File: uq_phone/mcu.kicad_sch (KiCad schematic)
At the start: 22 parts, among them J11 FTSH-105-XX-X-DV, U5 TXB0108RGYR, U6 TXB0108RGYR, U7 STM32H730VBTx

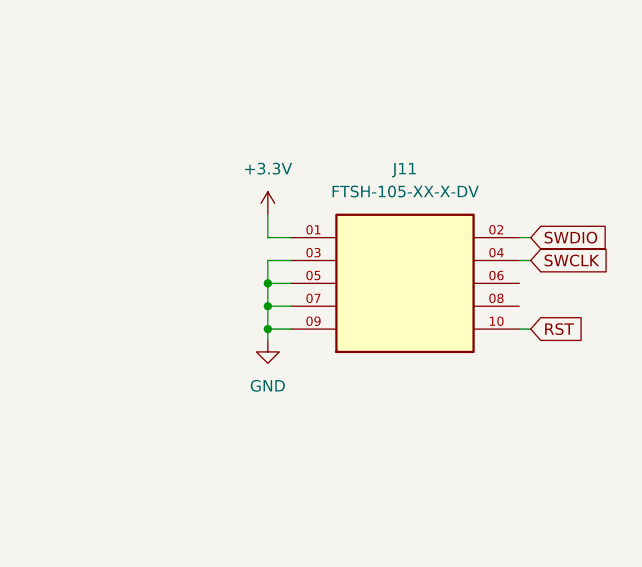
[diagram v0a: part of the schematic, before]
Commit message: Update LCD, Add Programer, Shrink Footprints
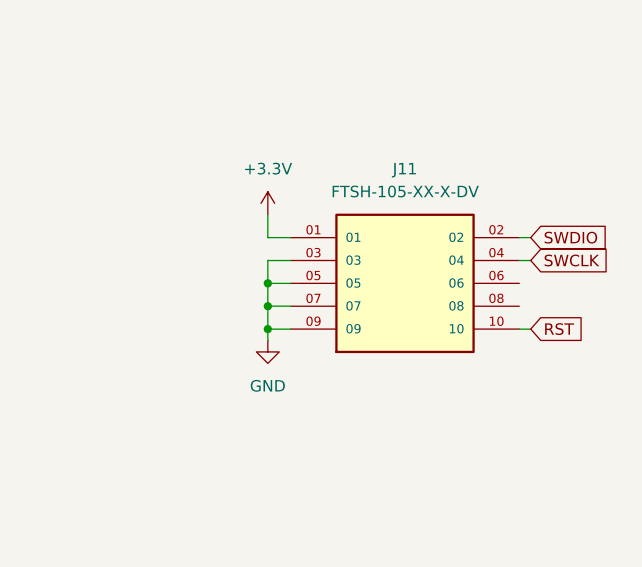
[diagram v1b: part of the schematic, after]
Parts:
- R26, R27, R28, R29: footprint Resistor_SMD:R_0603_1608Metric -> Resistor_SMD:R_0402_1005Metric

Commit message: Shrink More footprints, rearragment of PCB
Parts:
- C19, C20, C21, C22, C23, C24, C25, C26, C27, C28, C29, C30, C31: footprint Capacitor_SMD:C_0603_1608Metric -> Capacitor_SMD:C_0402_1005Metric

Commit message: Update PCB, minor changes
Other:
- note added: "CHECK PINOUT"
- note added: "MCU"
- note added: "Programmer"
- moved on the sheet: C19, C20, C21, C22, J11, U5, U6

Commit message: Arrange PCB
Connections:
- net MOB_PWR: no longer names the net of U7.93 (PB7)
- net MOB_RST renamed MOB_RST_CTL

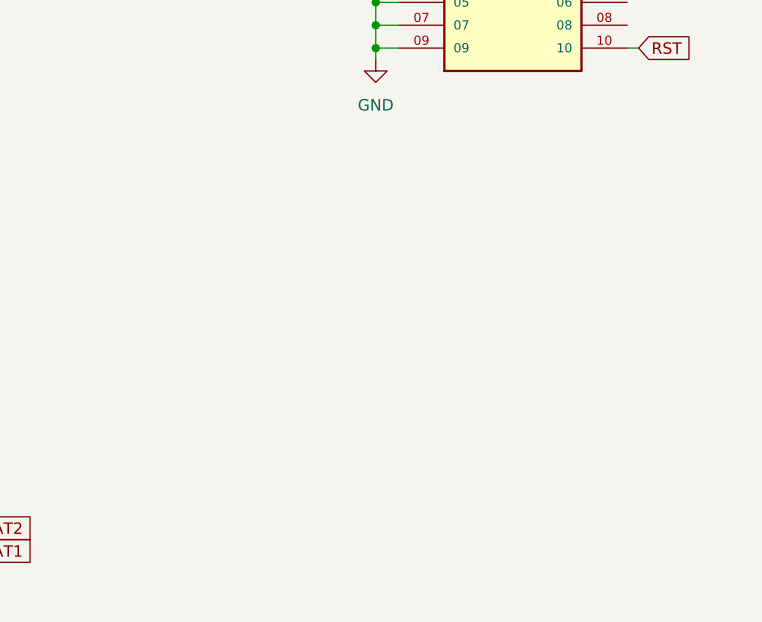
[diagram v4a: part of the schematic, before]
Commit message: Add LEDs, Inital Buttons
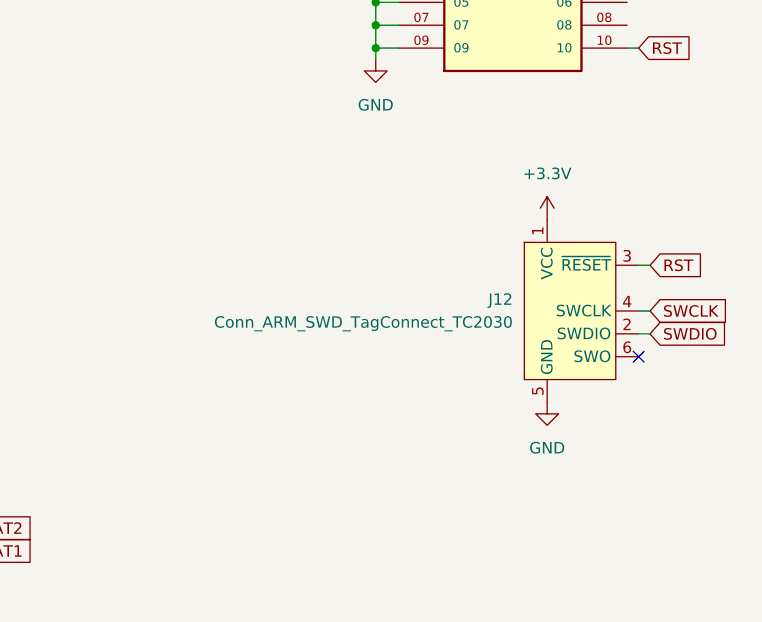
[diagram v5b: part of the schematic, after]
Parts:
- added J12: Conn_ARM_SWD_TagConnect_TC2030, Connector:Tag-Connect_TC2030-IDC-FP_2x03_P1.27mm_Vertical, symbol Connector:Conn_ARM_SWD_TagConnect_TC2030
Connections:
- net +3.3V: now also J12.1 (VCC)
- net GND: now also J12.5 (GND)
- net RST: now also J12.3 (~{RESET})
- net SWCLK: now also J12.4 (SWCLK)
- net SWDIO: now also J12.2 (SWDIO)
- no-connect marks 3 -> 4

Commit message: Routing Init
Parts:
- removed TP19: TestPoint, TestPoint:TestPoint_Pad_D1.0mm, symbol Connector:TestPoint
- renumbered C19 to C14, C20 to C15, C21 to C16, C22 to C17, C23 to C18, C24 to C19, C25 to C20, C26 to C21, C27 to C22, C28 to C23, C29 to C24, C30 to C25, C31 to C26, J11 to J5, J12 to J6, R26 to R24, R27 to R25, R28 to R26, R29 to R27
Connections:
- net AUD_SW_H: now also U6.14 (B6); no longer U6.12 (B8)
- net AUD_SW_L: now also U6.7 (A6); no longer U6.9 (A8)
- net MCU_AUD_BCLK_H: now also U6.13 (B7); no longer U6.14 (B6)
- net MCU_AUD_BCLK_L: now also U6.8 (A7); no longer U6.7 (A6)
- net MCU_AUD_OUT_L: now also U6.9 (A8); no longer U6.6 (A5)
- net MCU_AUD_OUT_L_H: now also U6.12 (B8); no longer U6.15 (B5)
- net MCU_AUD_SYNC_H: now also U6.15 (B5); no longer U6.13 (B7)
- net MCU_AUD_SYNC_L: now also U6.6 (A5); no longer U6.8 (A7)
- net MCU_DCD: now also U5.18 (B2), U7.59 (PD12); no longer U5.17 (B3), U7.60 (PD13)
- net MCU_DSR: now also U5.20 (B1); no longer U5.12 (B8)
- net MCU_DTR: now also U5.17 (B3), U7.60 (PD13); no longer U5.20 (B1), U7.59 (PD12)
- net MCU_RI: now also U5.12 (B8); no longer U5.16 (B4)
- net MCU_RXD: now also U5.16 (B4); no longer U5.18 (B2)
- net MOB_DCD: now also U5.3 (A2); no longer U5.4 (A3)
- net MOB_DSR: now also U5.1 (A1); no longer U5.9 (A8)
- net MOB_DTR: now also U5.4 (A3); no longer U5.1 (A1)
- net MOB_PWR_CTL: now also U7.36 (PB2)
- net MOB_RI: now also U5.9 (A8); no longer U5.5 (A4)
- net MOB_RST_CTL: now also U7.47 (PB11); no longer U7.91 (PB5)
- net MOB_RXD: now also U5.5 (A4); no longer U5.3 (A2)
- net MOB_WAKE_H: now also U7.35 (PB1); no longer U7.92 (PB6)

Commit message: Update routing
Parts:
- removed J5: FTSH-105-XX-X-DV, FTSH-105-XX-X-DV:SAMTEC_FTSH-105-XX-X-DV, symbol FTSH-105-XX-X-DV:FTSH-105-XX-X-DV
